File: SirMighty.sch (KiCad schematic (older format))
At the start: 40 parts, among them J1 Conn_01x20, J2 Conn_01x20, J3 USB_B_Micro, Q1 Q_DUAL_PMOS_S1G1D2S2G2D1, U1 ATmega1284P-MU, U2 AP7365-ADJ, U3 FT231XQ, U4 AP1117-50, Y1 20MHz

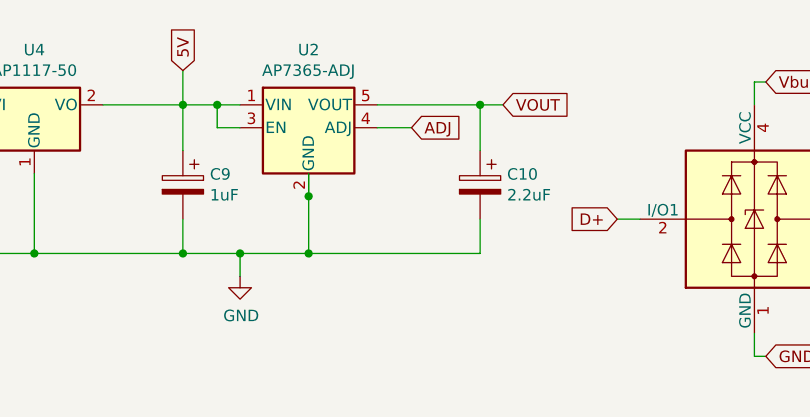
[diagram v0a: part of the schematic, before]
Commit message: LDO capacitors edited
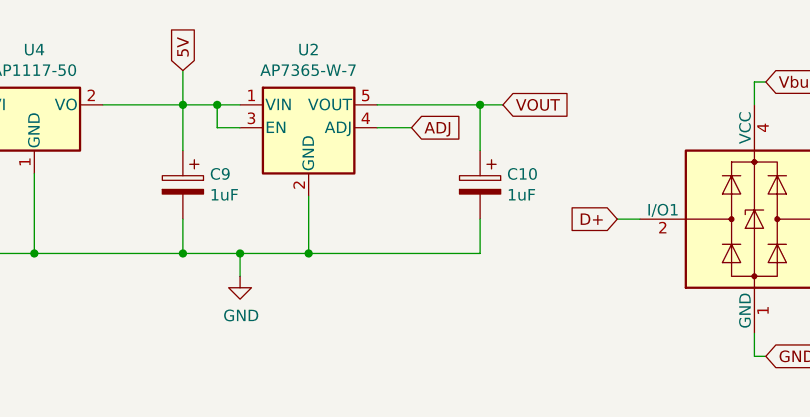
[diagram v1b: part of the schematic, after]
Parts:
- C10: value 2.2uF -> 1uF
- F1: footprint Resistor_SMD:R_0805_2012Metric -> Resistor_SMD:R_1206_3216Metric
- U2: value AP7365-ADJ -> AP7365-W-7
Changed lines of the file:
@@
 F 0 "F1" H 10288 4096 50  0000 L CNN
 F 1 "500mA" H 10288 4005 50  0000 L CNN
-F 2 "Resistor_SMD:R_0805_2012Metric" H 10250 3850 50  0001 L CNN
+F 2 "Resistor_SMD:R_1206_3216Metric" H 10250 3850 50  0001 L CNN
 F 3 "~" H 10200 4050 50  0001 C CNN
 	1    10200 4050
@@
 P 4800 1250
 F 0 "C10" H 4682 1296 50  0000 R CNN
-F 1 "2.2uF" H 4682 1205 50  0000 R CNN
+F 1 "1uF" H 4682 1205 50  0000 R CNN
 F 2 "Capacitor_SMD:C_0805_2012Metric_Pad1.15x1.40mm_HandSolder" H 4838 1100 50  0001 C CNN
 F 3 "~" H 4800 1250 50  0001 C CNN
@@
 Wire Wire Line
 	3500 900  3500 1100
-Wire Wire Line
-	4050 1200 4050 1300
-Connection ~ 4050 1300
 Text GLabel 1100 900  0    50   Input ~ 0
 VIN
 Wire Wire Line
 	4050 1300 4050 1550
-Wire Wire Line
-	4050 1550 4800 1550
 Connection ~ 10200 3750
 Wire Wire Line
@@
 P 4050 1000
 F 0 "U2" H 4050 1340 50  0000 C CNN
-F 1 "AP7365-ADJ" H 4050 1250 50  0000 C CNN
+F 1 "AP7365-W-7" H 4050 1250 50  0000 C CNN
 F 2 "Package_TO_SOT_SMD:SOT-23-5" H 4050 1325 50  0001 C CNN
 F 3 "https://www.diodes.com/assets/Datasheets/AP2204.pdf" H 4050 1100 50  0001 C CNN
@@
 Wire Wire Line
 	1200 1550 2000 1550
-Connection ~ 4050 1550
 Wire Wire Line
 	3500 1400 3500 1550
@@
 	3750 1650 3750 1550
 Connection ~ 3750 1550
-Wire Wire Line
-	3750 1550 4050 1550
 Wire Wire Line
 	8900 3100 9050 3100
@@
 	8000 3450 8000 3350
 Connection ~ 8000 3350
+Wire Wire Line
+	3750 1550 4050 1550
+Connection ~ 4050 1550
+Wire Wire Line
+	4050 1550 4800 1550
 $EndSCHEMATC

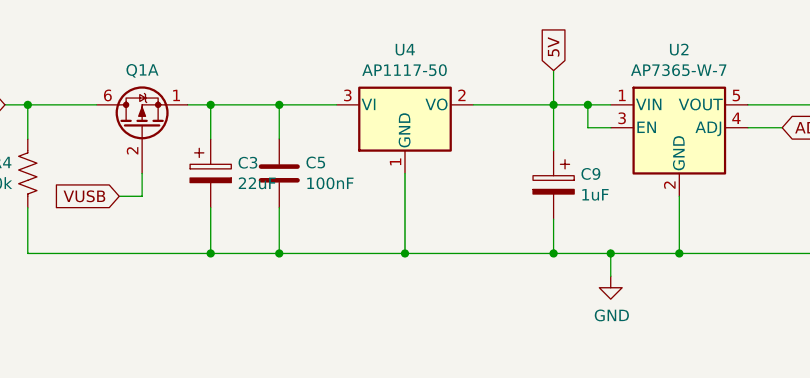
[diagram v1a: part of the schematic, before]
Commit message: Regulator changed from AP to AZ
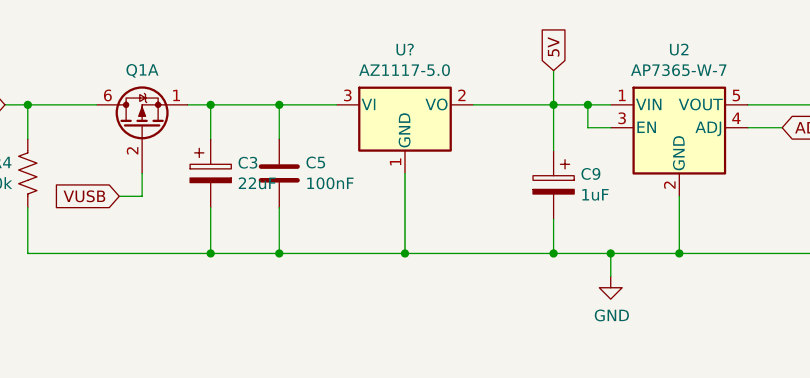
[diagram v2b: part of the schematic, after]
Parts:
- removed U4: AP1117-50, Package_TO_SOT_SMD:SOT-223-3_TabPin2, symbol Regulator_Linear:AP1117-50
- added U?: AZ1117-5.0, Package_TO_SOT_SMD:SOT-223-3_TabPin2, symbol Regulator_Linear:AZ1117-5.0
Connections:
- net 5V: now also U?.2 (VO)
- net GND: now also U?.1 (GND)
- net at C3.1, C5.1, Q1.1 (S): now also U?.3 (VI)
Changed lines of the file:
@@
 	8450 1850 8350 1850
-$Comp
-L Regulator_Linear:AP1117-50 U4
-U 1 1 5DCAAF50
-P 2850 900
-F 0 "U4" H 2850 1140 50  0000 C CNN
-F 1 "AP1117-50" H 2850 1050 50  0000 C CNN
-F 2 "Package_TO_SOT_SMD:SOT-223-3_TabPin2" H 2850 1100 50  0001 C CNN
-F 3 "http://www.diodes.com/datasheets/AP1117.pdf" H 2950 650 50  0001 C CNN
-	1    2850 900
-	1    0    0    -1
-$EndComp
 $Comp
 L Regulator_Linear:AP2204K-ADJ U2
@@
 Wire Wire Line
 	4050 1550 4800 1550
+$Comp
+L Regulator_Linear:AZ1117-5.0 U?
+U 1 1 5D8AFD92
+P 2850 900
+F 0 "U?" H 2850 1140 50  0000 C CNN
+F 1 "AZ1117-5.0" H 2850 1050 50  0000 C CNN
+F 2 "Package_TO_SOT_SMD:SOT-223-3_TabPin2" H 2850 1150 50  0001 C CIN
+F 3 "https://www.diodes.com/assets/Datasheets/AZ1117.pdf" H 2850 900 50  0001 C CNN
+	1    2850 900
+	1    0    0    -1
+$EndComp
 $EndSCHEMATC

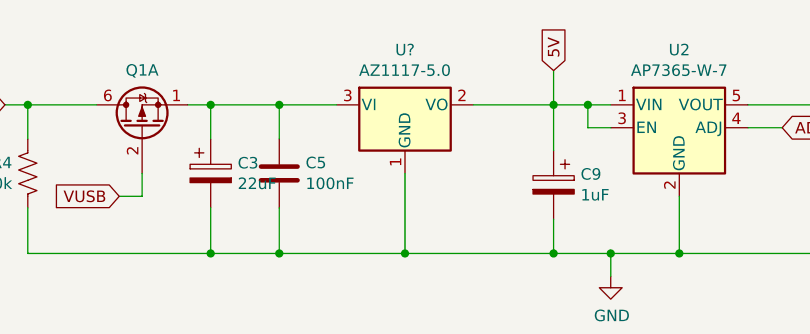
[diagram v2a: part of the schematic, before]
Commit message: Capacitor Footprint changed
3216 to 3512
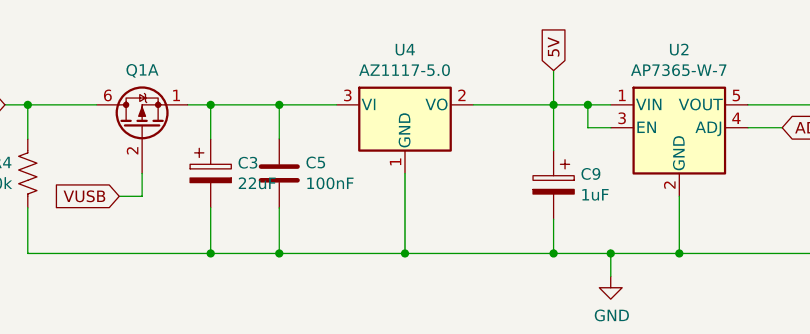
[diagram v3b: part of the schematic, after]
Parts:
- C3: footprint Capacitor_Tantalum_SMD:CP_EIA-3216-18_Kemet-A_Pad1.58x1.35mm_HandSolder -> Capacitor_Tantalum_SMD:CP_EIA-3528-12_Kemet-T
- gave numbers to parts that had none: 1
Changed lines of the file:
@@
 F 0 "C3" H 2118 1245 50  0000 L CNN
 F 1 "22uF" H 2118 1155 50  0000 L CNN
-F 2 "Capacitor_Tantalum_SMD:CP_EIA-3216-18_Kemet-A_Pad1.58x1.35mm_HandSolder" H 2038 1050 50  0001 C CNN
+F 2 "Capacitor_Tantalum_SMD:CP_EIA-3528-12_Kemet-T" H 2038 1050 50  0001 C CNN
 F 3 "~" H 2000 1200 50  0001 C CNN
 	1    2000 1200
@@
 	4050 1550 4800 1550
 $Comp
-L Regulator_Linear:AZ1117-5.0 U?
+L Regulator_Linear:AZ1117-5.0 U4
 U 1 1 5D8AFD92
 P 2850 900
-F 0 "U?" H 2850 1140 50  0000 C CNN
+F 0 "U4" H 2850 1140 50  0000 C CNN
 F 1 "AZ1117-5.0" H 2850 1050 50  0000 C CNN
 F 2 "Package_TO_SOT_SMD:SOT-223-3_TabPin2" H 2850 1150 50  0001 C CIN

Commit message: Page Settings Updated
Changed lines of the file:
@@
 encoding utf-8
 Sheet 1 1
-Title ""
-Date ""
-Rev ""
-Comp ""
-Comment1 ""
-Comment2 ""
+Title "SirMighty"
+Date "2019-08-11"
+Rev "1"
+Comp "SirBoard"
+Comment1 "www.SirBoard.com"
+Comment2 "ATMega1284 Based Dev Board"
 Comment3 ""
 Comment4 ""
@@
 U 1 1 5D524CE7
 P 4350 5400
-F 0 "U1" H 4350 3312 50  0000 C CNN
-F 1 "ATmega1284P-MU" H 4350 3222 50  0000 C CNN
+F 0 "U1" H 4775 3325 50  0000 C CNN
+F 1 "ATmega1284P-MU" H 4775 3400 50  0000 C CNN
 F 2 "Package_DFN_QFN:QFN-44-1EP_7x7mm_P0.5mm_EP5.2x5.2mm" H 4350 5400 50  0001 C CIN
 F 3 "http://ww1.microchip.com/downloads/en/DeviceDoc/Atmel-8272-8-bit-AVR-microcontroller-ATmega164A_PA-324A_PA-644A_PA-1284_P_datasheet.pdf" H 4350 5400 50  0001 C CNN
@@
 Wire Wire Line
 	5100 6700 4950 6700
-Wire Wire Line
-	3450 4700 3450 7500
-Wire Wire Line
-	3450 7500 4350 7500
 Wire Wire Line
 	4350 7500 4350 7400
@@
 MISO
 Wire Wire Line
-	7800 6050 6000 6050
-Wire Wire Line
-	6000 6050 6000 7500
-Wire Wire Line
-	6000 7500 4350 7500
-Connection ~ 7800 6050
-Connection ~ 4350 7500
-Wire Wire Line
 	10700 2000 10850 2000
 Wire Wire Line
@@
 	1    0    0    -1
 $EndComp
+$Comp
+L power:GND #PWR?
+U 1 1 5DEF7311
+P 4350 7500
+F 0 "#PWR?" H 4350 7250 50  0001 C CNN
+F 1 "GND" H 4355 7327 50  0000 C CNN
+F 2 "" H 4350 7500 50  0001 C CNN
+F 3 "" H 4350 7500 50  0001 C CNN
+	1    4350 7500
+	1    0    0    -1
+$EndComp
+$Comp
+L power:GND #PWR?
+U 1 1 5DF0D40E
+P 3450 4700
+F 0 "#PWR?" H 3450 4450 50  0001 C CNN
+F 1 "GND" H 3455 4527 50  0000 C CNN
+F 2 "" H 3450 4700 50  0001 C CNN
+F 3 "" H 3450 4700 50  0001 C CNN
+	1    3450 4700
+	1    0    0    -1
+$EndComp

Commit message: Part Numbers Added
Minor Board Revisions
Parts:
- added C12: 100nF, Capacitor_SMD:C_0603_1608Metric, symbol Device:C
- C1, C5, C7: Part (none) -> C42998
- C10, C9: Part (none) -> C396719
- C11: footprint Capacitor_SMD:C_0805_2012Metric_Pad1.15x1.40mm_HandSolder -> Capacitor_SMD:C_0603_1608Metric; Part (none) -> C42998
- C2, C4: Part (none) -> C105622
- C3: Part (none) -> C7199
- C6: Part (none) -> C100042
- C8: Part (none) -> C122643
- D0: Part (none) -> C193191
- D1: Part (none) -> C12333
- F1: Part (none) -> C89657
- J3: Part (none) -> C132560
- L1: Part (none) -> C99366
- PWR1: Part (none) -> C118330
- Q1: footprint Package_TO_SOT_SMD:SOT-363_SC-70-6 -> (none)
- Q1: Part (none) -> C332299
- R1, R2: Part (none) -> C325726
- R3: footprint Resistor_SMD:R_0805_2012Metric_Pad1.15x1.40mm_HandSolder -> Resistor_SMD:R_0603_1608Metric; Part (none) -> C99198
- R4: Part (none) -> C99198
- R5: Part (none) -> C304766
- R6: Part (none) -> C103426
- R7: Part (none) -> C163436
- RN1: Part (none) -> C164038
- RST1: Part (none) -> C231330
- RX1, TX1: Part (none) -> C205443
- U1: Part (none) -> 127-8233
- U2: Part (none) -> C264087
- U3: Part (none) -> 757-0045
- U4: Part (none) -> C99342
- Y1: value 20MHz -> 16MHz; Part (none) -> C32180
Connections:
- net 3.3V: now also U3.11 (~RESET), C12.2
- net GND: now also C12.1
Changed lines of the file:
@@
 Sheet 1 1
 Title "SirMighty"
-Date "2019-08-11"
-Rev "1"
+Date "2019-12-03"
+Rev "2"
 Comp "SirBoard"
 Comment1 "www.SirBoard.com"
@@
 F 0 "R3" H 9118 2896 50  0000 L CNN
 F 1 "10k" H 9118 2805 50  0000 L CNN
-F 2 "Resistor_SMD:R_0805_2012Metric_Pad1.15x1.40mm_HandSolder" V 9090 2840 50  0001 C CNN
+F 2 "Resistor_SMD:R_0603_1608Metric" V 9090 2840 50  0001 C CNN
 F 3 "~" H 9050 2850 50  0001 C CNN
+F 4 "C99198" H 9050 2850 50  0001 C CNN "Part"
 	1    9050 2850
 	-1   0    0    -1
@@
 F 2 "LED_SMD:LED_0603_1608Metric" H 7350 2550 50  0001 C CNN
 F 3 "~" H 7350 2550 50  0001 C CNN
+F 4 "C205443" H 7350 2550 50  0001 C CNN "Part"
 	1    7350 2550
 	1    0    0    -1
@@
 F 2 "Button_Switch_SMD:SW_SPST_B3U-1000P-B" H 8700 3300 50  0001 C CNN
 F 3 "~" H 8700 3300 50  0001 C CNN
+F 4 "C231330" H 8700 3100 50  0001 C CNN "Part"
 	1    8700 3100
 	-1   0    0    -1
@@
 F 2 "Inductor_SMD:L_0805_2012Metric_Pad1.15x1.40mm_HandSolder" H 4800 2950 50  0001 C CNN
 F 3 "~" H 4800 2950 50  0001 C CNN
+F 4 "C99366" V 4800 2950 50  0001 C CNN "Part"
 	1    4800 2950
 	0    1    -1   0
@@
 F 2 "Resistor_SMD:R_0603_1608Metric" V 9740 4590 50  0001 C CNN
 F 3 "~" H 9700 4600 50  0001 C CNN
+F 4 "C325726" V 9700 4600 50  0001 C CNN "Part"
 	1    9700 4600
 	0    1    -1   0
@@
 F 2 "Resistor_SMD:R_0603_1608Metric" V 9740 4790 50  0001 C CNN
 F 3 "~" H 9700 4800 50  0001 C CNN
+F 4 "C325726" V 9700 4800 50  0001 C CNN "Part"
 	1    9700 4800
 	0    1    -1   0
@@
 F 2 "LED_SMD:LED_0603_1608Metric" H 7350 2950 50  0001 C CNN
 F 3 "~" H 7350 2950 50  0001 C CNN
+F 4 "C205443" H 7350 2950 50  0001 C CNN "Part"
 	1    7350 2950
 	1    0    0    -1
@@
 F 2 "LED_SMD:LED_0603_1608Metric" H 7350 3350 50  0001 C CNN
 F 3 "~" H 7350 3350 50  0001 C CNN
+F 4 "C118330" H 7350 3350 50  0001 C CNN "Part"
 	1    7350 3350
 	-1   0    0    -1
@@
 F 2 "LED_SMD:LED_0603_1608Metric" H 7350 2200 50  0001 C CNN
 F 3 "~" H 7350 2200 50  0001 C CNN
+F 4 "C193191" H 7350 2200 50  0001 C CNN "Part"
 	1    7350 2200
 	-1   0    0    -1
@@
 F 2 "Resistor_SMD:R_Array_Convex_4x0603" V 6925 2800 50  0001 C CNN
 F 3 "~" H 6650 2800 50  0001 C CNN
+F 4 "C164038" V 6650 2800 50  0001 C CNN "Part"
 	1    6650 2800
 	0    1    1    0
@@
 F 2 "Resistor_SMD:R_1206_3216Metric" H 10250 3850 50  0001 L CNN
 F 3 "~" H 10200 4050 50  0001 C CNN
+F 4 "C89657" H 10200 4050 50  0001 C CNN "Part"
 	1    10200 4050
 	-1   0    0    -1
@@
 F 2 "Capacitor_Tantalum_SMD:CP_EIA-3216-12_Kemet-S" H 10038 5000 50  0001 C CNN
 F 3 "~" H 10000 5150 50  0001 C CNN
+F 4 "C122643" H 10000 5150 50  0001 C CNN "Part"
 	1    10000 5150
 	1    0    0    -1
@@
 F 2 "Package_DFN_QFN:QFN-20-1EP_4x4mm_P0.5mm_EP2.5x2.5mm" H 8400 4100 50  0001 C CNN
 F 3 "http://www.ftdichip.com/Products/ICs/FT231X.html" H 7900 4950 50  0001 C CNN
+F 4 "757-0045" H 7900 4950 50  0001 C CNN "Part"
 	1    7900 4950
 	-1   0    0    -1
@@
 F 2 "Capacitor_SMD:C_0603_1608Metric" H 9088 5000 50  0001 C CNN
 F 3 "~" H 9050 5150 50  0001 C CNN
+F 4 "C105622" H 9050 5150 50  0001 C CNN "Part"
 	1    9050 5150
 	-1   0    0    -1
@@
 F 2 "Connector_USB:USB_Micro-B_Molex_47346-0001" H 10800 4600 50  0001 C CNN
 F 3 "~" H 10800 4600 50  0001 C CNN
+F 4 "C132560" H 10650 4650 50  0001 C CNN "Part"
 	1    10650 4650
 	-1   0    0    -1
@@
 F 2 "Capacitor_SMD:C_0603_1608Metric" H 10238 5000 50  0001 C CNN
 F 3 "~" H 10200 5150 50  0001 C CNN
+F 4 "C100042" H 10200 5150 50  0001 C CNN "Part"
 	1    10200 5150
 	1    0    0    -1
@@
 Connection ~ 8550 6050
 Wire Wire Line
-	8550 6050 9050 6050
-$Comp
-L Device:C C11
-U 1 1 5DA62F39
-P 6850 4750
-F 0 "C11" H 6965 4796 50  0000 L CNN
-F 1 "100nF" H 6965 4705 50  0000 L CNN
-F 2 "Capacitor_SMD:C_0805_2012Metric_Pad1.15x1.40mm_HandSolder" H 6888 4600 50  0001 C CNN
-F 3 "~" H 6850 4750 50  0001 C CNN
-	1    6850 4750
-	0    -1   1    0
-$EndComp
+	8550 6050 8650 6050
 Wire Wire Line
 	7200 4750 7000 4750
@@
 F 2 "Capacitor_SMD:C_0805_2012Metric_Pad1.15x1.40mm_HandSolder" H 4838 1100 50  0001 C CNN
 F 3 "~" H 4800 1250 50  0001 C CNN
+F 4 "C396719" H 4800 1250 50  0001 C CNN "Part"
 	1    4800 1250
 	-1   0    0    -1
@@
 F 2 "Capacitor_SMD:C_0805_2012Metric_Pad1.15x1.40mm_HandSolder" H 3538 1100 50  0001 C CNN
 F 3 "~" H 3500 1250 50  0001 C CNN
+F 4 "C396719" H 3500 1250 50  0001 C CNN "Part"
 	1    3500 1250
 	-1   0    0    -1
@@
 P 2850 4000
 F 0 "Y1" V 2895 4110 50  0000 L CNN
-F 1 "20MHz" V 2805 4110 50  0000 L CNN
+F 1 "16MHz" V 2805 4110 50  0000 L CNN
 F 2 "Crystal:Resonator_SMD_muRata_CSTxExxV-3Pin_3.0x1.1mm" H 2825 4000 50  0001 C CNN
 F 3 "~" H 2825 4000 50  0001 C CNN
+F 4 "C32180" V 2850 4000 50  0001 C CNN "Part"
 	1    2850 4000
 	0    1    -1   0
@@
 F 2 "Capacitor_SMD:C_0603_1608Metric" H 9388 5000 50  0001 C CNN
 F 3 "~" H 9350 5150 50  0001 C CNN
+F 4 "C105622" H 9350 5150 50  0001 C CNN "Part"
 	1    9350 5150
 	1    0    0    -1
@@
 F 2 "Package_TO_SOT_SMD:SOT-143" H 6060 1400 50  0001 C CNN
 F 3 "https://assets.nexperia.com/documents/data-sheet/PRTR5V0U2X.pdf" H 6060 1400 50  0001 C CNN
+F 4 "C12333" H 6000 1400 50  0001 C CNN "Part"
 	1    6000 1400
 	1    0    0    -1
@@
 F 0 "Q1" V 8701 1550 50  0000 C CNN
 F 1 "Q_DUAL_PMOS_S1G1D2S2G2D1" V 8701 1550 50  0001 C CNN
-F 2 "Package_TO_SOT_SMD:SOT-363_SC-70-6" H 8500 1550 50  0001 C CNN
+F 2 "" H 8500 1550 50  0001 C CNN
 F 3 "~" H 8500 1550 50  0001 C CNN
 	2    8450 1550
@@
 F 2 "Package_TO_SOT_SMD:SOT-23-5" H 4050 1325 50  0001 C CNN
 F 3 "https://www.diodes.com/assets/Datasheets/AP2204.pdf" H 4050 1100 50  0001 C CNN
+F 4 "C264087" H 4050 1000 50  0001 C CNN "Part"
 	1    4050 1000
 	1    0    0    -1
@@
 F 2 "Resistor_SMD:R_0603_1608Metric" V 1340 2190 50  0001 C CNN
 F 3 "~" H 1300 2200 50  0001 C CNN
+F 4 "C304766" V 1300 2200 50  0001 C CNN "Part"
 	1    1300 2200
 	0    1    -1   0
@@
 F 2 "" H 1750 1000 50  0001 C CNN
 F 3 "~" H 1750 1000 50  0001 C CNN
+F 4 "C332299" V 1700 1000 50  0001 C CNN "Part"
 	1    1700 1000
 	0    -1   -1   0
@@
 F 2 "Resistor_SMD:R_0603_1608Metric" V 1240 1190 50  0001 C CNN
 F 3 "~" H 1200 1200 50  0001 C CNN
+F 4 "C99198" H 1200 1200 50  0001 C CNN "Part"
 	1    1200 1200
 	-1   0    0    -1
@@
 F 2 "Capacitor_Tantalum_SMD:CP_EIA-3528-12_Kemet-T" H 2038 1050 50  0001 C CNN
 F 3 "~" H 2000 1200 50  0001 C CNN
+F 4 "C7199" H 2000 1200 50  0001 C CNN "Part"
 	1    2000 1200
 	1    0    0    -1
@@
 F 2 "Capacitor_SMD:C_0603_1608Metric" H 2338 1050 50  0001 C CNN
 F 3 "~" H 2300 1200 50  0001 C CNN
+F 4 "C42998" H 2300 1200 50  0001 C CNN "Part"
 	1    2300 1200
 	1    0    0    -1
@@
 F 2 "Resistor_SMD:R_0603_1608Metric" V 1340 2890 50  0001 C CNN
 F 3 "~" H 1300 2900 50  0001 C CNN
+F 4 "C103426" V 1300 2900 50  0001 C CNN "Part"
 	1    1300 2900
 	0    1    -1   0
@@
 F 2 "Resistor_SMD:R_0603_1608Metric" V 2290 2540 50  0001 C CNN
 F 3 "~" H 2250 2550 50  0001 C CNN
+F 4 "C163436" V 2250 2550 50  0001 C CNN "Part"
 	1    2250 2550
 	0    1    -1   0
@@
 F 2 "Package_DFN_QFN:QFN-44-1EP_7x7mm_P0.5mm_EP5.2x5.2mm" H 4350 5400 50  0001 C CIN
 F 3 "http://ww1.microchip.com/downloads/en/DeviceDoc/Atmel-8272-8-bit-AVR-microcontroller-ATmega164A_PA-324A_PA-644A_PA-1284_P_datasheet.pdf" H 4350 5400 50  0001 C CNN
+F 4 "127-8233" H 4350 5400 50  0001 C CNN "Part"
 	1    4350 5400
 	1    0    0    -1
@@
 F 2 "Capacitor_SMD:C_0603_1608Metric" H 3488 4400 50  0001 C CNN
 F 3 "~" H 3450 4550 50  0001 C CNN
+F 4 "C42998" H 3450 4550 50  0001 C CNN "Part"
 	1    3450 4550
 	-1   0    0    -1
@@
 F 2 "Capacitor_SMD:C_0603_1608Metric" H 5138 3000 50  0001 C CNN
 F 3 "~" H 5100 3150 50  0001 C CNN
+F 4 "C42998" H 5100 3150 50  0001 C CNN "Part"
 	1    5100 3150
 	1    0    0    -1
@@
 F 2 "Package_TO_SOT_SMD:SOT-223-3_TabPin2" H 2850 1150 50  0001 C CIN
 F 3 "https://www.diodes.com/assets/Datasheets/AZ1117.pdf" H 2850 900 50  0001 C CNN
+F 4 "C99342" H 2850 900 50  0001 C CNN "Part"
 	1    2850 900
 	1    0    0    -1
 $EndComp
 $Comp
-L power:GND #PWR?
+L power:GND #PWR0104
 U 1 1 5DEF7311
 P 4350 7500
-F 0 "#PWR?" H 4350 7250 50  0001 C CNN
+F 0 "#PWR0104" H 4350 7250 50  0001 C CNN
 F 1 "GND" H 4355 7327 50  0000 C CNN
 F 2 "" H 4350 7500 50  0001 C CNN
@@
 $EndComp
 $Comp
-L power:GND #PWR?
+L power:GND #PWR0109
 U 1 1 5DF0D40E
 P 3450 4700
-F 0 "#PWR?" H 3450 4450 50  0001 C CNN
+F 0 "#PWR0109" H 3450 4450 50  0001 C CNN
 F 1 "GND" H 3455 4527 50  0000 C CNN
 F 2 "" H 3450 4700 50  0001 C CNN
@@
 	1    0    0    -1
 $EndComp
+Wire Wire Line
+	8600 4950 8650 4950
+Wire Wire Line
+	8650 4950 8650 4350
+$Comp
+L Device:C C12
+U 1 1 5DE9C688
+P 8650 5450
+F 0 "C12" H 8765 5496 50  0000 L CNN
+F 1 "100nF" H 8765 5405 50  0000 L CNN
+F 2 "Capacitor_SMD:C_0603_1608Metric" H 8688 5300 50  0001 C CNN
+F 3 "~" H 8650 5450 50  0001 C CNN
+F 4 "C42998" H 8650 5450 50  0001 C CNN "Part"
+	1    8650 5450
+	1    0    0    1
+$EndComp
+Wire Wire Line
+	8650 5300 8650 4950
+Connection ~ 8650 4950
+Wire Wire Line
+	8650 5600 8650 6050
+Connection ~ 8650 6050
+Wire Wire Line
+	8650 6050 9050 6050
+$Comp
+L Device:C C11
+U 1 1 5E1E7179
+P 6850 4750
+F 0 "C11" V 7000 4825 50  0000 L CNN
+F 1 "100nF" V 7000 4525 50  0000 L CNN
+F 2 "Capacitor_SMD:C_0603_1608Metric" H 6888 4600 50  0001 C CNN
+F 3 "~" H 6850 4750 50  0001 C CNN
+F 4 "C42998" H 6850 4750 50  0001 C CNN "Part"
+	1    6850 4750
+	0    -1   1    0
+$EndComp
 $EndSCHEMATC
